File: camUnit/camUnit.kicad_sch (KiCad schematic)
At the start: 3 parts

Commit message: yes
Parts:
- added U3: ~, Library:m1n, symbol vincent:m1n
- gave numbers to parts that had none: 2
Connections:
- net at U1.37 (PC6): now also U3.16 (TX)
- net at U1.38 (PC7): now also U3.2 (RX)
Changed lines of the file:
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@@
 	(generator_version "8.0")
 	(paper "A4")
+	(wire
+		(pts
+			(xy 170.18 87.63) (xy 173.99 87.63)
+		)
+		(stroke
+			(width 0)
+			(type default)
+		)
+	)
+	(wire
+		(pts
+			(xy 166.37 90.17) (xy 173.99 90.17)
+		)
+		(stroke
+			(width 0)
+			(type default)
+		)
+	)
+	(wire
+		(pts
+			(xy 154.94 87.63) (xy 166.37 87.63)
+		)
+		(stroke
+			(width 0)
+			(type default)
+		)
+	)
+	(wire
+		(pts
+			(xy 154.94 85.09) (xy 170.18 85.09)
+		)
+		(stroke
+			(width 0)
+			(type default)
+		)
+	)
+	(wire
+		(pts
+			(xy 166.37 87.63) (xy 166.37 90.17)
+		)
+		(stroke
+			(width 0)
+			(type default)
+		)
+	)
+	(wire
+		(pts
+			(xy 170.18 85.09) (xy 170.18 87.63)
+		)
+		(stroke
+			(width 0)
+			(type default)
+		)
+	)
 	(symbol
 		(lib_id "vincent:STM32F446RE")
@@
 		(dnp no)
 		(fields_autoplaced yes)
-		(property "Reference" "U?"
+		(property "Reference" "U2"
 			(at 208.28 60.96 0)
 			(effects
@@
 			(project ""
 				(path "/6130ea90-01d1-434c-a614-117c329ecbc2"
-					(reference "U?")
+					(reference "U2")
 					(unit 1)
 				)
@@
 		(dnp no)
 		(fields_autoplaced yes)
-		(property "Reference" "U?"
+		(property "Reference" "U1"
 			(at 133.35 62.23 0)
 			(effects
@@
 			(project ""
 				(path "/6130ea90-01d1-434c-a614-117c329ecbc2"
-					(reference "U?")
+					(reference "U1")
 					(unit 2)
 				)
@@
 		(dnp no)
 		(fields_autoplaced yes)
-		(property "Reference" "U?"
+		(property "Reference" "U1"
 			(at 93.98 59.69 0)
 			(effects
@@
 			(project ""
 				(path "/6130ea90-01d1-434c-a614-117c329ecbc2"
-					(reference "U?")
+					(reference "U1")
 					(unit 1)
 				)
+			)
+		)
+	)
+	(symbol
+		(lib_id "vincent:m1n")
+		(at 166.37 90.17 0)
+		(unit 1)
+		(exclude_from_sim no)
+		(in_bom yes)
+		(on_board yes)
+		(dnp no)
+		(fields_autoplaced yes)
+		(property "Reference" "U3"
+			(at 177.8 91.4399 0)
+			(effects
+				(font
+					(size 1.27 1.27)
+				)
+				(justify left)
+			)
+		)
+		(property "Value" "~"
+			(at 177.8 92.71 0)
+			(effects
+				(font
+					(size 1.27 1.27)
+				)
+				(justify left)
+			)
+		)
+		(property "Footprint" "Library:m1n"
+			(at 166.37 90.17 0)
+			(effects
+				(font
+					(size 1.27 1.27)
+				)
+				(hide yes)
+			)
+		)
+		(property "Datasheet" ""
+			(at 166.37 90.17 0)
+			(effects
+				(font
+					(size 1.27 1.27)
+				)
+				(hide yes)
+			)
+		)
+		(property "Description" ""
+			(at 166.37 90.17 0)
+			(effects
+				(font
+					(size 1.27 1.27)
+				)
+				(hide yes)
+			)
+		)
+		(pin "2"
+		)
+		(pin "25"
+		)
+		(pin "27"
+		)
+		(pin "16"
+		)
+		(instances
+			(project ""
+				(path "/6130ea90-01d1-434c-a614-117c329ecbc2"
+					(reference "U3")
+					(unit 1)
+				)

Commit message: Camunit
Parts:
- removed U1, U2: STM32F446RET, Package_QFP:LQFP-64_10x10mm_P0.5mm, symbol vincent:STM32F446RE
- removed U3: ~, Library:m1n, symbol vincent:m1n
- added J1: Conn_01x08, symbol Connector_Generic:Conn_01x08
- added SW2: SW_SPDT, Library:SS12D00G3, symbol Switch:SW_SPDT
- added U2: ~, 2024l3:OpenMV_RT, symbol Library:OpenMV_RT
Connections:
- new net +5V FILT: SW2.1 (A)
- new net CAM PWR: SW2.2 (B), U2.29 (VIN)
- new net GNDREF: U2.15 (GND), U2.31 (GND)
- no-connect marks 0 -> 1
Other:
- added sheet TNSY (untitled.kicad_sch)

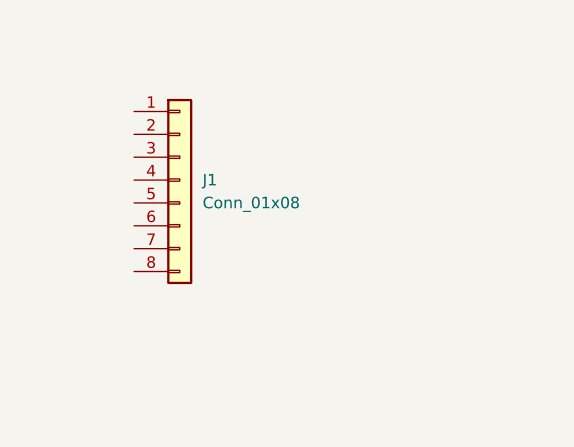
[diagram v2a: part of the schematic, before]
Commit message: m1n footprint
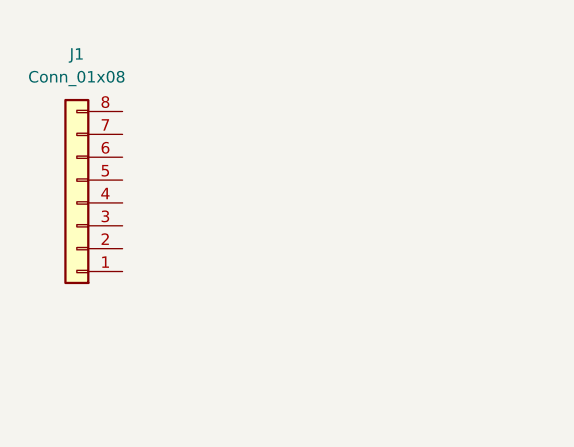
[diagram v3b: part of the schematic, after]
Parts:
- J1: footprint (none) -> Connector_JST:JST_XH_B8B-XH-AM_1x08_P2.50mm_Vertical
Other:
- moved on the sheet: J1
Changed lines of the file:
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@@
 	(symbol
 		(lib_id "Connector_Generic:Conn_01x08")
-		(at 34.29 48.26 0)
+		(at 22.86 50.8 180)
 		(unit 1)
 		(exclude_from_sim no)
@@
 		(fields_autoplaced yes)
 		(property "Reference" "J1"
-			(at 36.83 48.2599 0)
+			(at 22.86 34.29 0)
 			(effects
 				(font
 					(size 1.27 1.27)
 				)
-				(justify left)
 			)
 		)
 		(property "Value" "Conn_01x08"
-			(at 36.83 50.7999 0)
+			(at 22.86 36.83 0)
 			(effects
 				(font
 					(size 1.27 1.27)
 				)
-				(justify left)
 			)
 		)
-		(property "Footprint" ""
-			(at 34.29 48.26 0)
+		(property "Footprint" "Connector_JST:JST_XH_B8B-XH-AM_1x08_P2.50mm_Vertical"
+			(at 22.86 50.8 0)
 			(effects
 				(font
@@
 		)
 		(property "Datasheet" "~"
-			(at 34.29 48.26 0)
+			(at 22.86 50.8 0)
 			(effects
 				(font
@@
 		)
 		(property "Description" "Generic connector, single row, 01x08, script generated (kicad-library-utils/schlib/autogen/connector/)"
-			(at 34.29 48.26 0)
+			(at 22.86 50.8 0)
 			(effects
 				(font

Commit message: Camunit
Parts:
- removed SW2: SW_SPDT, Library:SS12D00G3, symbol Switch:SW_SPDT
- removed U2: ~, 2024l3:OpenMV_RT, symbol Library:OpenMV_RT
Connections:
- net +5V FILT: now also J1.8 (Pin_8)
- net GNDREF: now also J1.1 (Pin_1), J1.2 (Pin_2)
- net TOF TX: now reaches J1.3 (Pin_3)
- net TOF RX: now reaches J1.4 (Pin_4)
- net CAM RX: now reaches J1.5 (Pin_5)
- net CAM TX: now reaches J1.6 (Pin_6)
- net +3V3 FILT: now reaches J1.7 (Pin_7)
- no-connect marks 1 -> 0
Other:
- added sheet TOF (tof.kicad_sch)
- sheet TNSY: file untitled.kicad_sch -> TNSY.kicad_sch

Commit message: Cam Layer
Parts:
- added SW1: SW_SPDT, Library:SS12D00G3, symbol Switch:SW_SPDT
- added U1: ~, Library:OpenMV_RT, symbol Library:OpenMV_RT
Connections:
- net +5V FILT: now also SW1.1 (A)
- net CAM RX: now also U1.10 (P5-RX/SDA/PWM)
- net CAM TX: now also U1.8 (P4-TX/SCL/PWM)
- net GNDREF: now also U1.15 (GND), U1.31 (GND)
- new net CAM PWR: SW1.2 (B), U1.29 (VIN)
- new net CAM RST: U1.17 (RST)
- no-connect marks 0 -> 23
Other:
- removed sheet TNSY

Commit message: CamUnit
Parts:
- added H1, H2, H3, H4: MountingHole, MountingHole:MountingHole_3.2mm_M3_Pad_Via, symbol Mechanical:MountingHole

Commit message: shrink pcb
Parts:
- J1: footprint Connector_JST:JST_XH_B8B-XH-AM_1x08_P2.50mm_Vertical -> Connector_JST:JST_XH_B8B-XH-A_1x08_P2.50mm_Vertical
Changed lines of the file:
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@@
 	(label "CAM PWR"
 		(at 163.83 64.77 0)
-		(fields_autoplaced yes)
 		(effects
 			(font
@@
 	(label "CAM PWR"
 		(at 185.42 44.45 0)
-		(fields_autoplaced yes)
 		(effects
 			(font
@@
 	(label "CAM RST"
 		(at 165.1 26.67 0)
-		(fields_autoplaced yes)
 		(effects
 			(font
@@
 			)
 		)
-		(property "Footprint" "Connector_JST:JST_XH_B8B-XH-AM_1x08_P2.50mm_Vertical"
+		(property "Footprint" "Connector_JST:JST_XH_B8B-XH-A_1x08_P2.50mm_Vertical"
 			(at 22.86 50.8 0)
 			(effects

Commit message: CamUnit
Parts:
- added C10, C11, C8, C9: 2u2, Library:cap0603, symbol Device:C
- added FB1, FB2: 100R, Library:fb0805, symbol Device:FerriteBead
- added Q1: IRLML6344TRPBF, Library:SOT95P237X112-3N, symbol Library:IRLML6344TRPBF
- added R5, R6: 1k, Library:res0603, symbol Device:R
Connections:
- net +3V3 FILT: now also SW1.2 (B), C9.1, FB1.2
- net +5V FILT: now also C11.1, FB2.2, R6.1; no longer SW1.1 (A)
- net CAM PWR: now also Q1.3 (D), R6.2; no longer SW1.2 (B)
- net GNDREF: now also C10.2, C11.2, C8.2, C9.2, Q1.2 (S), R5.2
- new net: Q1.1 (G), R5.1, SW1.1 (A)
- new net +3V3: C8.1, FB1.1
- new net +5V: C10.1, FB2.1
